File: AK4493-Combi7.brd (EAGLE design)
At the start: 177.8 x 174.9 mm, 239 parts, among them IC1 LT3042, IC3 AK4493, IC4 LT3042, IC4A SN74ABT273DBR, IC5 LT3042, IC6 LT3042, IC7 LT3042, IC8 LT3042, IC9 AK4493, J15 XR2A-0811-N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

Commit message: progress
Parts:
- moved BD1 0.15 mm to (120.1, 149.8)
- moved C10A2 0.15 mm to (96.9, 99.6)
- moved C10A3 0.15 mm to (158.1, 108.3)
- moved C11A 0.15 mm to (141.9, 93.5)
- moved C11B 0.15 mm to (82.1, 115.8)
- moved C12A2 0.15 mm to (94.2, 98.1)
- moved C12A3 0.15 mm to (159.5, 105.6)
- moved C13A 0.15 mm to (168.4, 108.4)
- moved C13B 0.15 mm to (97.0, 89.3)
- moved C14A2 0.15 mm to (88.3, 101.0)
- moved C14A3 0.15 mm to (156.7, 99.7)
- moved C15A 0.15 mm to (162.2, 94.4)
- moved C15B 0.15 mm to (79.6, 98.9)
- moved C16A2 0.15 mm to (89.7, 99.7)
- moved C16A3 0.15 mm to (157.9, 101.0)
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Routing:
- net VCC: track 416.5 -> 484.0 mm
- net N$94: track 24.5 -> 41.1 mm
- net N$45: track 24.5 -> 41.1 mm
- net N$37: track 25.3 -> 40.4 mm
- net N$92: track 28.0 -> 41.6 mm
- net N$114: track 31.9 -> 41.7 mm
- net N$93: track 31.9 -> 41.7 mm
- net N$91: track 25.4 -> 33.9 mm
- net N$116: track 25.4 -> 33.3 mm
- net N$131: track 68.1 -> 65.2 mm
- net 66.3VAC/2: track 309.0 -> 308.1 mm
- net +240VDC: track 475.4 -> 474.8 mm
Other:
- board size 177.8 x 174.9 mm -> 178 x 174.9 mm

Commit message: Progress
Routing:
- net +240VDC: track 474.8 -> 480.1 mm, vias 1 -> 3
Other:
- outline, holes or cut-outs redrawn

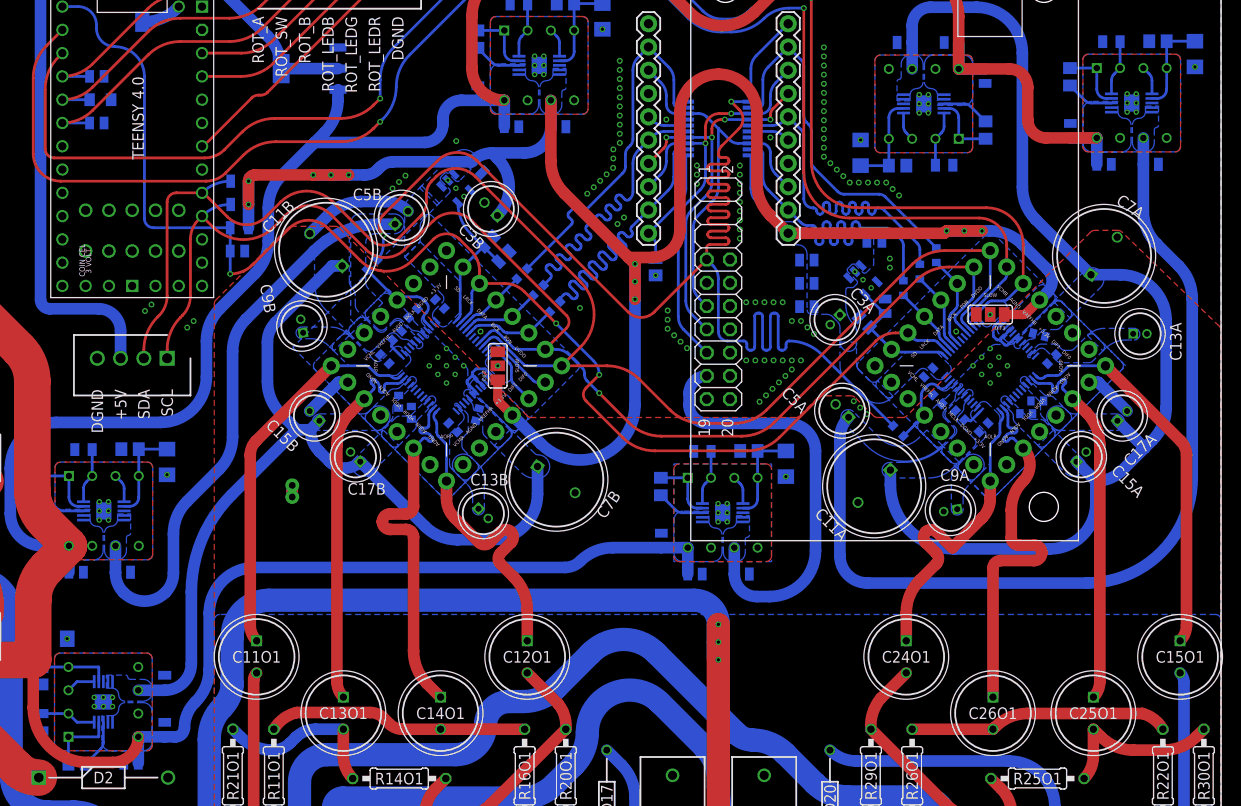
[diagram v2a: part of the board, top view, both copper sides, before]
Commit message: Update AK4493-Combi7.brd
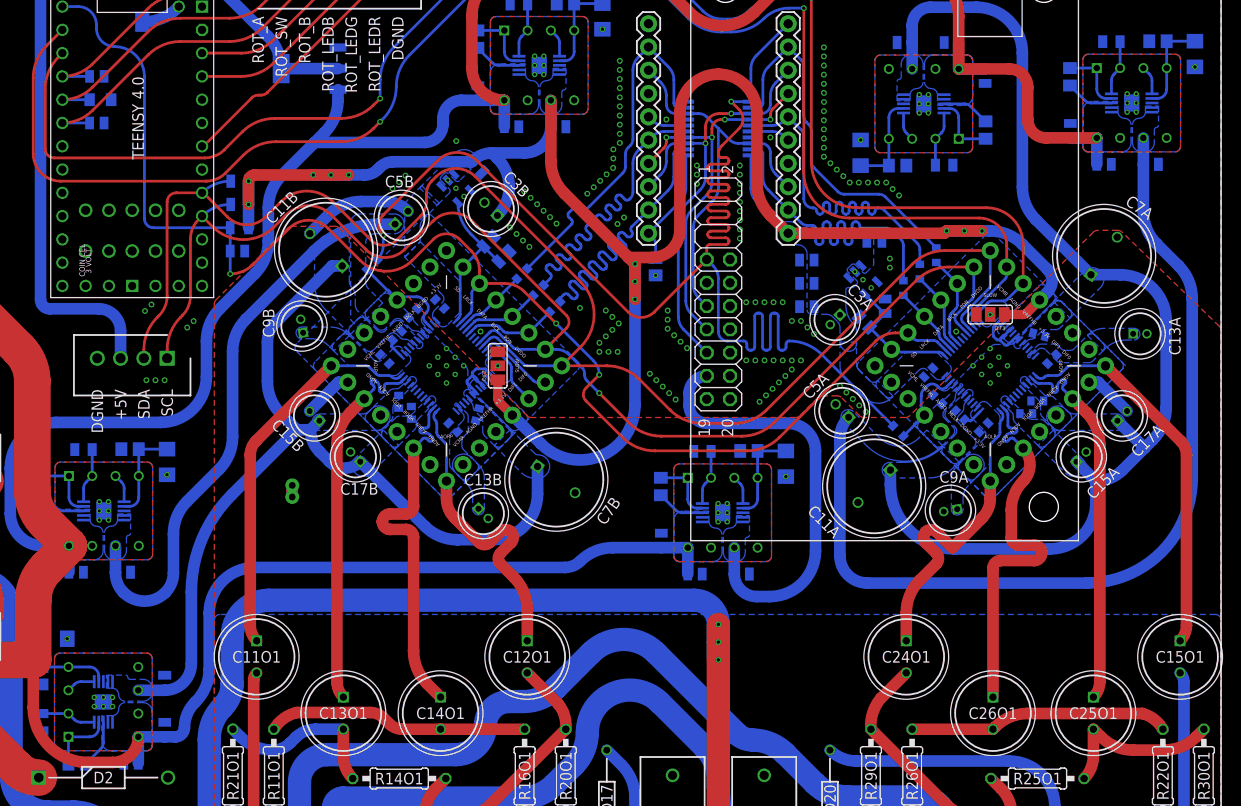
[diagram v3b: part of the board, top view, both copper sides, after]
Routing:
- net N$17: track 7.84 -> 7.25 mm
- net N$103: track 10.9 -> 10.3 mm
- net DGND: vias 100 -> 129
